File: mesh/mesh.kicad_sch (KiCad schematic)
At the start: 73 parts, among them J1 u.FL, J2 USB-C plug, SW1 USER, U1 RP2040, U2 SX1262IMLTRT, U3 W25Q32JVSSIQ, U4 PE4259-63, U5 ME6211C33M5G, U6 LP5907MFX-3.3, U7 USBLC6-2SC6, Y1 12MHz CL10p, Y2 32MHz TCXO 3.0V clipped-sine

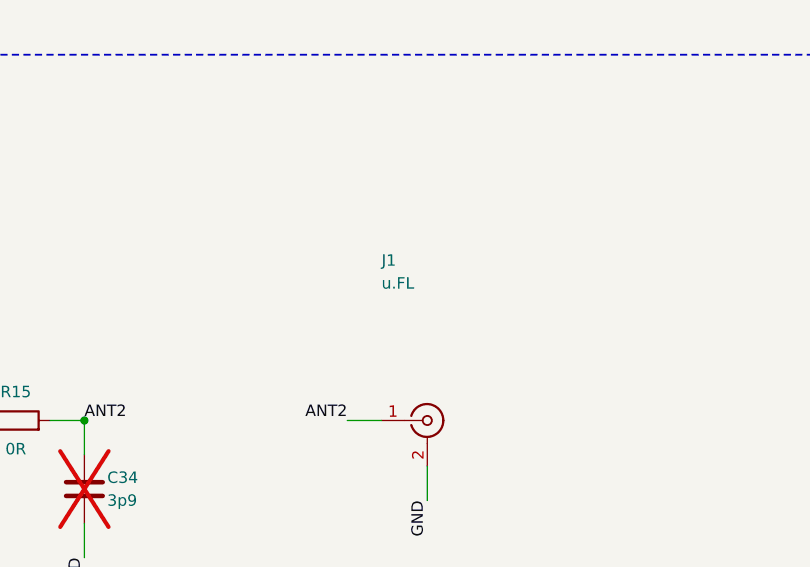
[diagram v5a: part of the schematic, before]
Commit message: Antenna: a real right-angle SMA jack, and a correction to why edge launches were rejected
The reason on file for avoiding a board-edge SMA was wrong. It said the Taoglas
EMPCB.SMAFSTJ.B.HT "caps at 0.79 mm" against a fab that delivers 0.72-0.88 mm. Its
specification table actually says 0.8 mm; only the footprint page says 0.79, and 0.79 mm
IS 0.031 in -- the number the industry uses for a 0.8 mm board, not a machined cliff.
Adafruit sell the same part class as "for 0.8mm / 0.031 Slim PCBs".

The real objection is different, and it applies to every edge launch rather than to one
part: tightening an SMA to its own spec torque of 0.57 N.m puts roughly 134 MPa of shear
into a 20 x 0.8 mm FR-4 strip, which is past FR-4's shear strength. The whip's weight was
never the problem -- safety factor around 130 -- the mating torque is.

BWSMA-KWE-Z001 answers both. Four ground legs and the centre pin are THROUGH HOLE, so
mating torque is carried by plated barrels through all four layers rather than by surface
pads or a clamp on a 0.8 mm edge, and board thickness stops being a parameter at all. It
is a right-angle jack, so the antenna axis lies in the board plane, which is what a stick
wants. LCSC has 130,155 at $0.51 against $3.75-4.01 for the edge launches -- and it is at
the distributor the owner already buys from, which matters on a hand-sourced board.
KiCad already ships the footprint, so nothing has to be authored.

It replaces the u.FL receptacle and its bulkhead pigtail, which existed only to dodge a
thickness conflict that turns out not to bind. Standard SMA female, not RP-SMA:
Meshtastic whips are SMA male.

Still worth doing in the enclosure: capture the connector body, so repeated mating does
not put the torque into the board alone.

Co-Authored-By: Claude Opus 5 (1M context) <noreply@anthropic.com>
Claude-Session: https://claude.ai/code/session_01L6RoqgW9x4s4XgQCvcFbCH
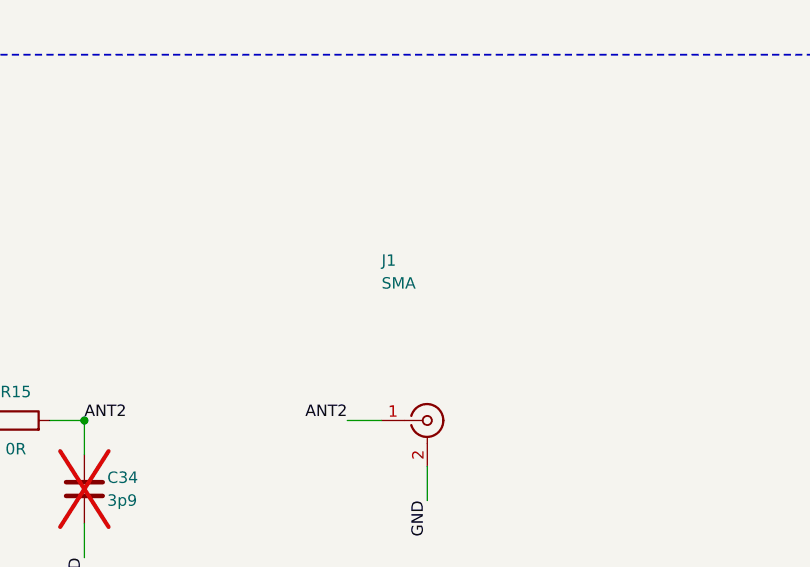
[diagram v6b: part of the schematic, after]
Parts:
- J1: value u.FL -> SMA; footprint Connector_Coaxial:U.FL_Hirose_U.FL-R-SMT-1_Vertical -> Connector_Coaxial:SMA_BAT_Wireless_BWSMA-KWE-Z001; LCSC C88373 -> C496551; MPN U.FL-R-SMT-1(10) -> BWSMA-KWE-Z001; Manufacturer Hirose -> BAT Wireless
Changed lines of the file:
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@@
 			)
 		)
-		(property "Value" "u.FL"
+		(property "Value" "SMA"
 			(at 322.58 327.66 0)
 			(show_name no)
@@
 			)
 		)
-		(property "Footprint" "Connector_Coaxial:U.FL_Hirose_U.FL-R-SMT-1_Vertical"
+		(property "Footprint" "Connector_Coaxial:SMA_BAT_Wireless_BWSMA-KWE-Z001"
 			(at 327.66 342.9 0)
 			(hide yes)
@@
 			)
 		)
-		(property "Description" "u.FL RF receptacle, SMT. Mates to a u.FL-to-SMA(F) bulkhead pigtail; ~30 mating cycles rated."
+		(property "Description" "SMA(F) right-angle jack, through-hole. Hand-fit after reflow. The enclosure should still capture the body so repeated mating torque does not load the board alone."
 			(at 327.66 342.9 0)
 			(hide yes)
@@
 			)
 		)
-		(property "MPN" "U.FL-R-SMT-1(10)"
+		(property "MPN" "BWSMA-KWE-Z001"
 			(at 327.66 342.9 0)
 			(hide yes)
@@
 			)
 		)
-		(property "Manufacturer" "Hirose"
+		(property "Manufacturer" "BAT Wireless"
 			(at 327.66 342.9 0)
 			(hide yes)
@@
 			)
 		)
-		(property "LCSC" "C88373"
+		(property "LCSC" "C496551"
 			(at 327.66 342.9 0)
 			(hide yes)

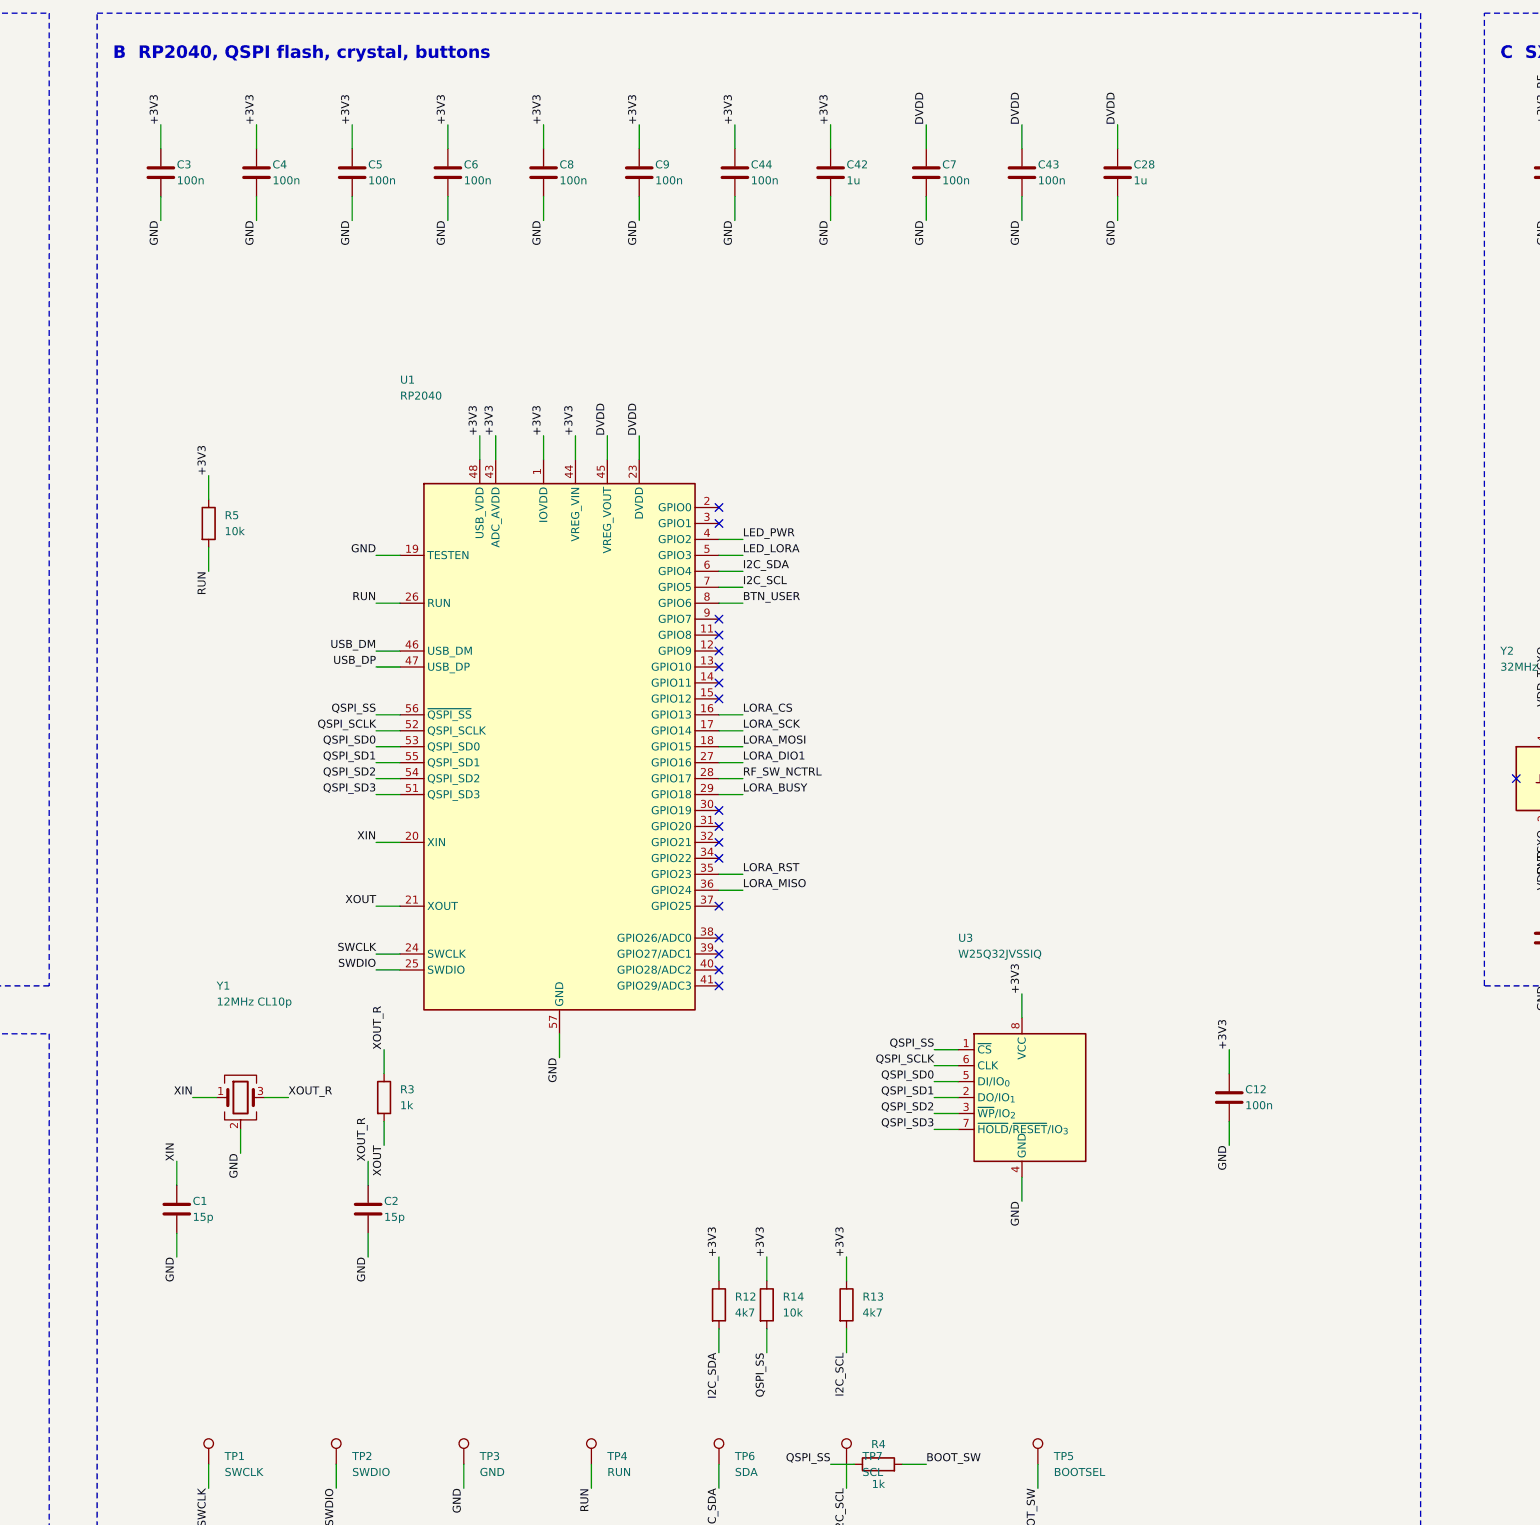
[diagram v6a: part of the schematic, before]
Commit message: RP2354A: the flash moves into the package
The owner asked twice for no second memory chip, so U1 becomes RP2354A -- an RP2350A die
with a Winbond W25Q16JVWI 2 MB flash die stacked in the same QFN-60 package. U3 and its
decoupling are gone, and so is the entire failure class that made us reject the
GD25Q32E: a flash that accepts only a one-byte 01h status-register write cannot have its
quad-enable bit set by the stock boot2, and the board would enumerate, accept a UF2, and
never run. That cannot happen to a die Raspberry Pi qualified themselves.

2 MB is enough, measured rather than assumed. Meshtastic's released pico2 image is
978,688 B against 1,536 kB of sketch space with the standard 0.5 MB LittleFS -- 62% used,
roughly three to four years of headroom at the observed growth rate.

Firmware support checked before committing to it, since that was the real risk:
Meshtastic has a first-class variants/rp2350/ tree with five environments, RP2350 is in
the CI matrix, firmware-rp2350-*.zip ships in every recent release, and
src/platform/rp2xx0/ is a shared RP2040+RP2350 layer with zero ARCH_RP2350 conditionals.
RP2354 is never named upstream but does not need to be -- identical pinout to RP2350A,
and a 2 MB RP2350A target already exists in-tree. This needs a variant.h and a
platformio.ini, not core work. Bluetooth is still absent, exactly as on RP2040.

Be honest about the cost: this did NOT shrink the BOM. RP2350's core supply is a BUCK,
not the simple LDO RP2040 had, and Raspberry Pi are prescriptive about it -- 3.3 uH
+/-20% fully shielded, DCR <= 250 mOhm, Isat >= 1.5 A, plus a 33 ohm filter into
VREG_AVDD and 4.7 uF at the input, the output and VREG_AVDD. RP2354 also needs its own
100 nF on QSPI_IOVDD, which feeds the internal flash die and must be 2.97-3.63 V. Net:
35 -> 36 line items, 64 -> 67 fitted placements. What was actually bought is the boot
failure mode gone, one fewer silicon vendor, and a SOIC-8 plus six QSPI traces off a
20 mm-wide board.

L2 is MPN3012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
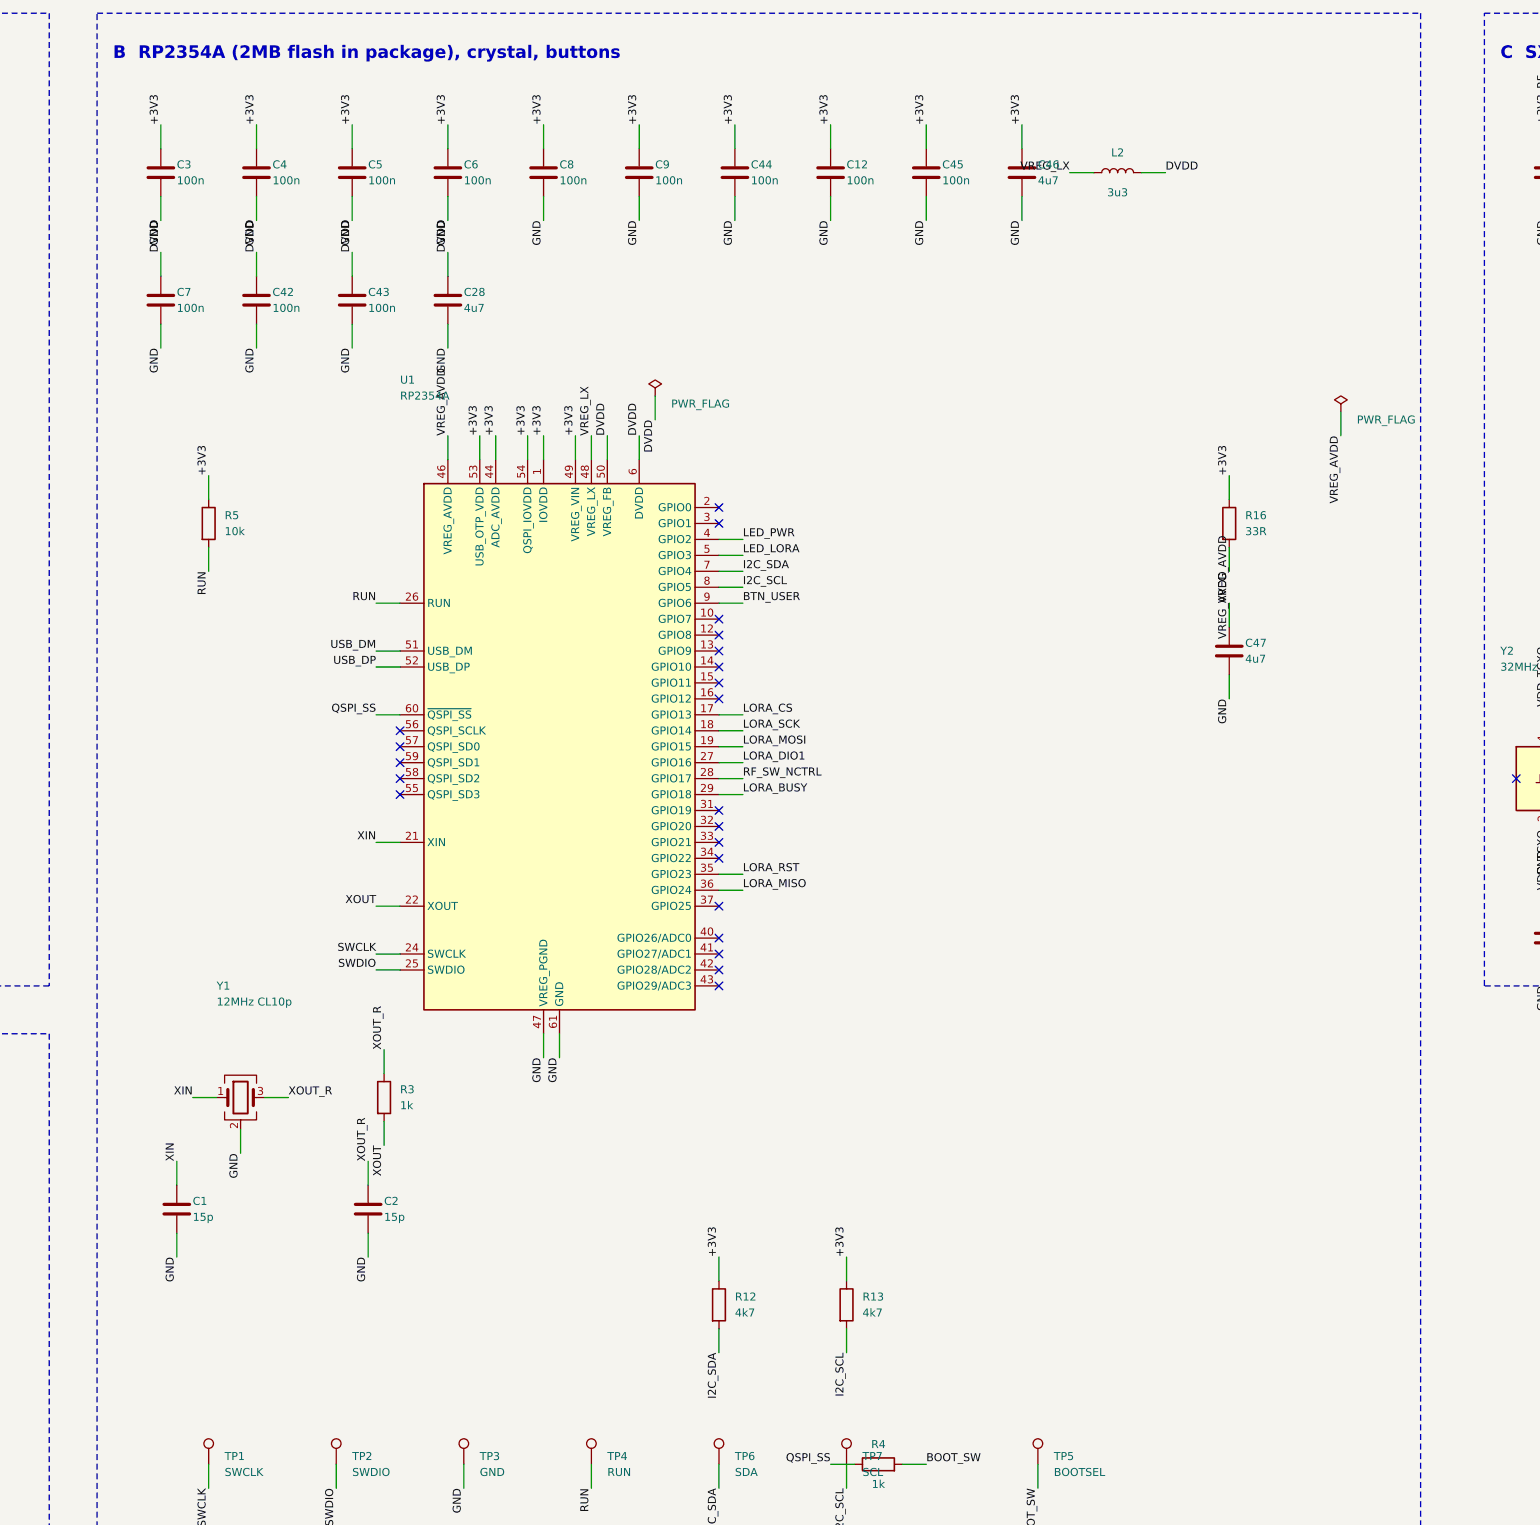
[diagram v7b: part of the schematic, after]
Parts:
- removed R14: 10k, Resistor_SMD:R_0402_1005Metric, symbol Device:R
- removed U3: W25Q32JVSSIQ, Package_SO:SOIC-8_5.3x5.3mm_P1.27mm, symbol Memory_Flash:W25Q32JVSS
- added C45: 100n, Capacitor_SMD:C_0402_1005Metric, symbol Device:C
- added C46, C47: 4u7, Capacitor_SMD:C_0603_1608Metric, symbol Device:C
- added L2: 3u3, Inductor_SMD:L_Cenker_CKCS3012, symbol Device:L
- added R16: 33R, Resistor_SMD:R_0402_1005Metric, symbol Device:R
- C28: value 1u -> 4u7; footprint Capacitor_SMD:C_0402_1005Metric -> Capacitor_SMD:C_0603_1608Metric; LCSC C52923 -> C19666; MPN CL05A105KA5NQNC -> CL10A475KO8NNNC; Voltage 25V -> 16V
- C42: value 1u -> 100n; Dielectric X5R -> X7R; LCSC C52923 -> C1525; MPN CL05A105KA5NQNC -> CL05B104KO5NNNC; Voltage 25V -> 16V
- U1: value RP2040 -> RP2354A; footprint zach:RP2040-QFN-56-1EP_7x7mm_P0.4mm_EP-vias -> zach:RP2354A-QFN-60-1EP_7x7mm_P0.4mm_EP-vias; symbol MCU_RaspberryPi:RP2040 -> MCU_RaspberryPi:RP2354A; LCSC C2040 -> C41378174; MPN RP2040 -> RP2354A
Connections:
- net QSPI_SCLK is gone; now on net USB_DP: U1.52 (USB_DP)
- net QSPI_SD0 is gone; now on net +3V3: U1.53 (USB_OTP_VDD)
- net QSPI_SD2 is gone; now on net +3V3: U1.54 (QSPI_IOVDD)
- net QSPI_SD3 is gone; now on net USB_DM: U1.51 (USB_DM)
- net +3V3: now also U1.11 (IOVDD), U1.20 (IOVDD), U1.30 (IOVDD), U1.38 (IOVDD), U1.45 (IOVDD), C45.1, C46.1, R16.1; no longer C42.1, U1.10 (IOVDD), U1.22 (IOVDD), U1.33 (IOVDD), U1.42 (IOVDD), U1.43 (ADC_AVDD), U1.48 (USB_VDD)
- net BTN_USER: now also U1.9 (GPIO6); no longer U1.8 (GPIO6)
- net DVDD: now also C42.1, U1.39 (DVDD), U1.6 (DVDD), L2.2; no longer U1.45 (VREG_VOUT)
- net GND: now also U1.47 (VREG_PGND), U1.61 (GND), C45.2, C46.2, C47.2; no longer U1.19 (TESTEN), U1.57 (GND)
- net I2C_SCL: now also U1.8 (GPIO5); no longer U1.7 (GPIO5)
- net I2C_SDA: now also U1.7 (GPIO4); no longer U1.6 (GPIO4)
- net LORA_CS: now also U1.17 (GPIO13); no longer U1.16 (GPIO13)
- net LORA_MOSI: now also U1.19 (GPIO15); no longer U1.18 (GPIO15)
- net LORA_SCK: now also U1.18 (GPIO14); no longer U1.17 (GPIO14)
- net QSPI_SS: now also U1.60 (~{QSPI_SS}); no longer U1.56 (~{QSPI_SS})
- net USB_DM: no longer U1.46 (USB_DM)
- net USB_DP: no longer U1.47 (USB_DP)
- net XIN: now also U1.21 (XIN); no longer U1.20 (XIN)
- net XOUT: now also U1.22 (XOUT); no longer U1.21 (XOUT)
- net QSPI_SD1: no longer names the net of U1.55 (QSPI_SD3)
- new net VREG_AVDD: C47.1, R16.2, U1.46 (VREG_AVDD)
- new net VREG_LX: L2.1, U1.48 (VREG_LX)
- no-connect marks 23 -> 28
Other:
- note added: "B RP2354A (2MB flash in package), crystal, buttons"
- note removed: "B RP2040, QSPI flash, crystal, buttons"
- moved on the sheet: C12, C28, C42, C43, C7

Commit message: Author the exact MPN3012S land rather than substituting a generic 3012
L2's footprint was the one assignment still marked unverified: a generic 3012-size land
standing in for a part whose drawing nobody had read. Pulled the manufacturer datasheet
(LCSC C52024124) and transcribed the Recommended Land Pattern table -- a (gap) = 1.00,
b (pad width) = 1.10, c (pad length) = 2.7, so pad centres sit at +/-1.05mm.

None of KiCad's three stock 3012 lands actually matches it. L_Cenker_CKCS3012, which was
assigned, has the right centres and the right pad length but 1.4mm-wide pads -- 0.3mm
over spec, which closes the inter-pad gap from 1.00 to 0.70mm directly underneath a
conductive metal-alloy body. L_Abracon_ASPI-3012S and L_APV_ANR3012 both place their pads
at +/-1.15mm centres instead.

Close enough to work, probably. But "probably" is not what the footprint field should
mean, and the whole land is eight numbers.

Every footprint on the board is now either an exact-MPN KiCad part, an IPC-standard
passive land, or authored here against a manufacturer drawing.

Co-Authored-By: Claude Opus 5 (1M context) <noreply@anthropic.com>
Claude-Session: https://claude.ai/code/session_01L6RoqgW9x4s4XgQCvcFbCH
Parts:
- L2: footprint Inductor_SMD:L_Cenker_CKCS3012 -> zach:L_MPN3012S_3.0x3.0mm
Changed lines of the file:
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@@
 			)
 		)
-		(property "Footprint" "Inductor_SMD:L_Cenker_CKCS3012"
+		(property "Footprint" "zach:L_MPN3012S_3.0x3.0mm"
 			(at 370.84 40.64 270)
 			(hide yes)
@@
 			)
 		)
-		(property "Description" "RP2350 core buck inductor: 3.3uH +/-20% shielded, 135mOhm, Isat 1.7A. Polarity/orientation per the datasheet. VERIFY the land pattern against the MPN3012S drawing before fab -- the footprint here is a generic 3012 land."
+		(property "Description" "RP2350 core buck inductor: 3.3uH +/-20% shielded, 135mOhm, Isat 1.7A. Land pattern transcribed from the manufacturer datasheet: pads 1.10 x 2.7mm at +/-1.05, gap 1.00."
 			(at 370.84 40.64 270)
 			(hide yes)
